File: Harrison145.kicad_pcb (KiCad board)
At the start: 2 copper layers, 85 x 55 mm, 150 parts, among them J1 PITCH ANTENNA, J2 VOLUME ANTENNA, J3 GROUND POINT, J4 LINE OUT, J5 9V IN, Q1 MMBT3906, Q10 SMP5484, Q11 MMBT3906, Q12 MMBT3906, Q13 SMP5484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

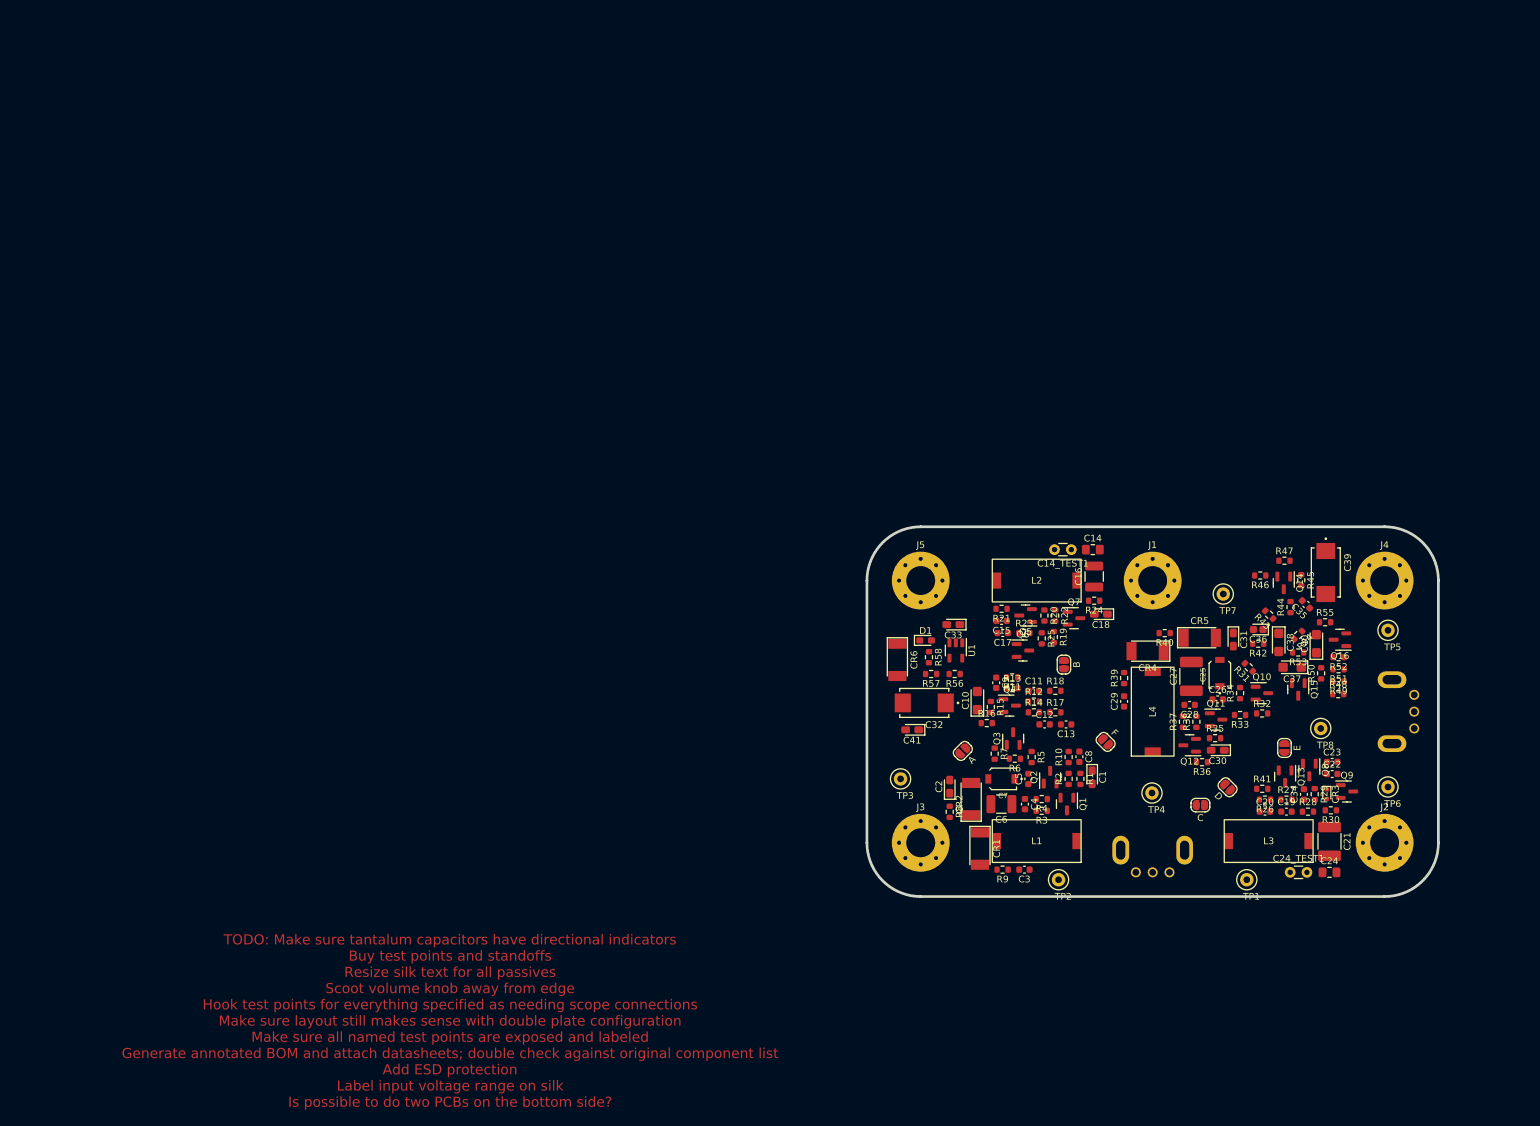
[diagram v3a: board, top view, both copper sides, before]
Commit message: Mostly routed
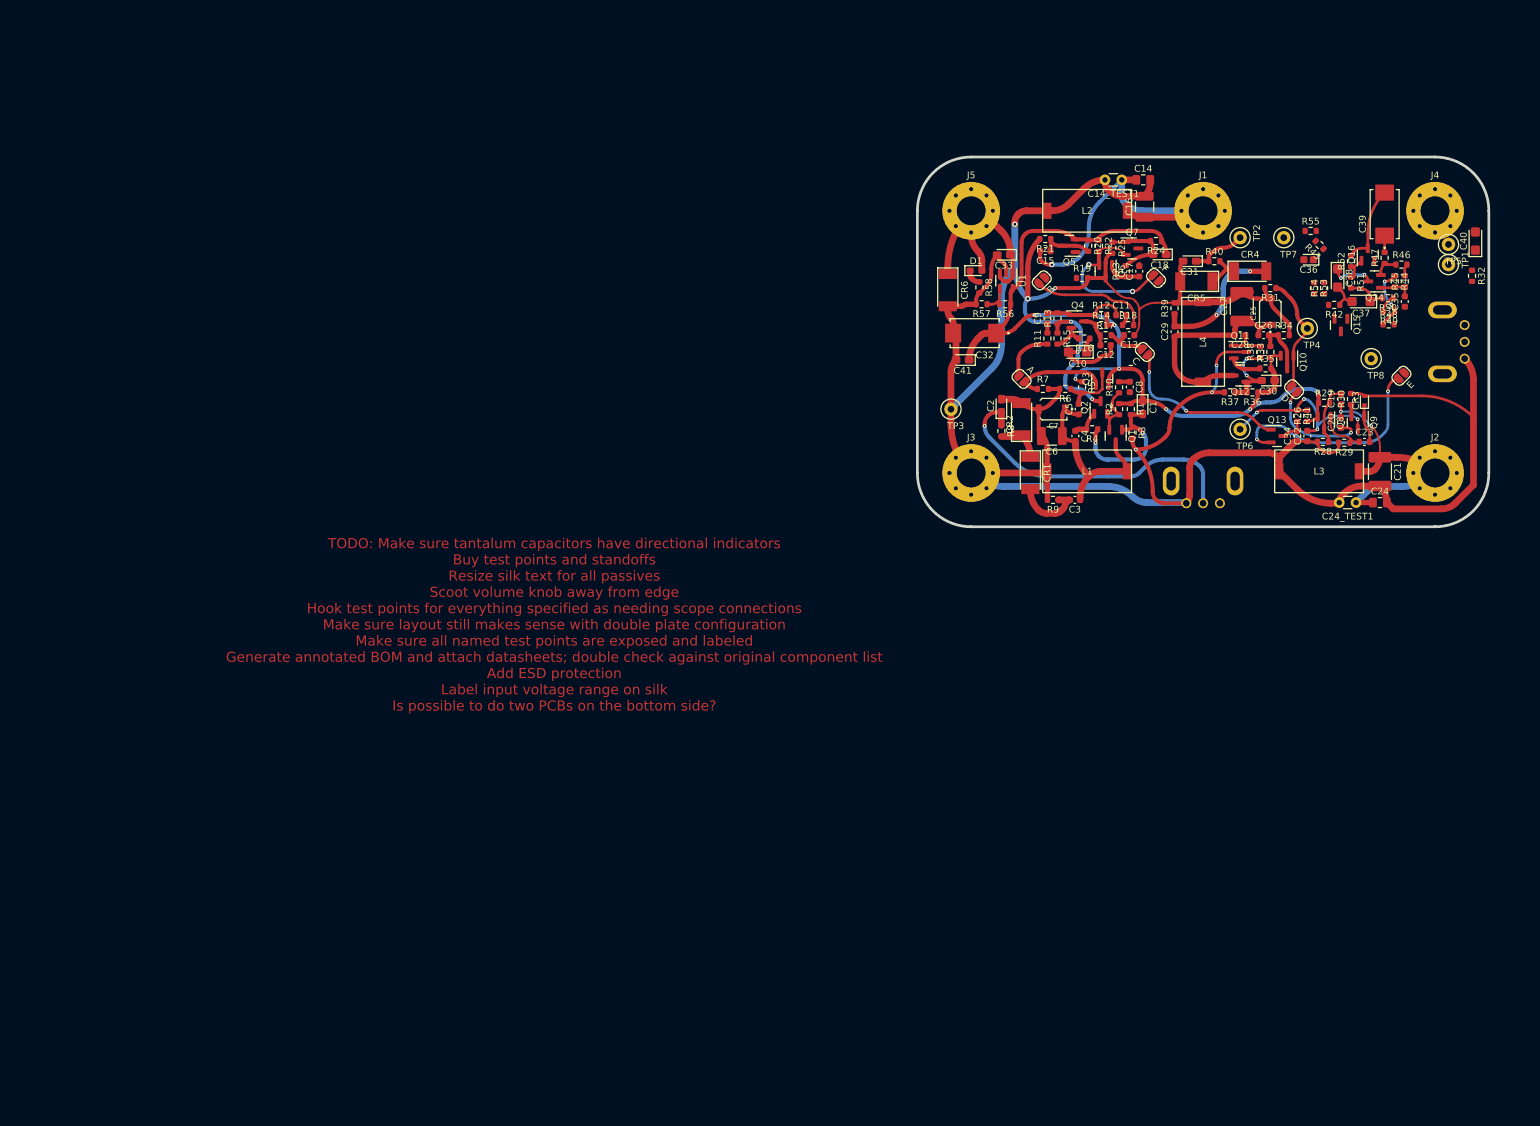
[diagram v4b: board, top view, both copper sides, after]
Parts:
- moved TP2 99.2 mm to (188.5, 64.0), turned to 90 degrees
- moved TP1 96.3 mm to (219.5, 68.0), turned to 90 degrees
- moved RV1 91.5 mm to (221.9, 79.5), turned to -90 degrees
- moved TP4 72.9 mm to (198.5, 77.5)
- moved R32 72.2 mm to (223.0, 69.7), turned to -90 degrees
- moved JP6 69.4 mm to (176.0, 70.0)
- moved JP3 67.9 mm to (174.3, 81.0), turned to -45 degrees
- moved C40 64.4 mm to (223.5, 64.5)
- moved C19 61.9 mm to (203.5, 88.0), turned to 90 degrees
- moved R30 61.2 mm to (205.0, 88.0), turned to 90 degrees
- moved JP4 60.0 mm to (196.5, 86.5)
- moved R27 59.3 mm to (201.0, 88.6)
- moved R25 59.0 mm to (169.5, 65.5)
- moved R16 59.0 mm to (165.3, 79.0), turned to 180 degrees
- moved C20 59.0 mm to (203.5, 91.5), turned to 90 degrees
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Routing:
- net GND: track 0.00 -> 452.2 mm, vias 0 -> 9
- net +7.5V: track 0.00 -> 152.5 mm, vias 0 -> 9
- net Net-(C14-Pad1): track 0.00 -> 54.7 mm, vias 0 -> 1
- net Net-(C2-Pad1): track 0.00 -> 47.6 mm, vias 0 -> 1
- net Net-(C19-Pad1): track 0.00 -> 41.1 mm, vias 0 -> 2
- net +9V: track 0.00 -> 35.7 mm
- net E: track 0.00 -> 32.8 mm, vias 0 -> 2
- net Net-(C25-Pad1): track 0.00 -> 31.8 mm
- net Net-(C3-Pad1): track 0.00 -> 28.7 mm
- net Net-(C22-Pad2): track 0.00 -> 28.5 mm, vias 0 -> 4
- net C: track 0.00 -> 25.3 mm, vias 0 -> 2
- net F: track 0.00 -> 23.0 mm, vias 0 -> 2
- net Net-(C1-Pad2): track 0.00 -> 21.8 mm, vias 0 -> 2
- net Net-(C29-Pad2): track 0.00 -> 20.6 mm, vias 0 -> 2
- net Net-(Q10-Pad1): track 0.00 -> 18.2 mm
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
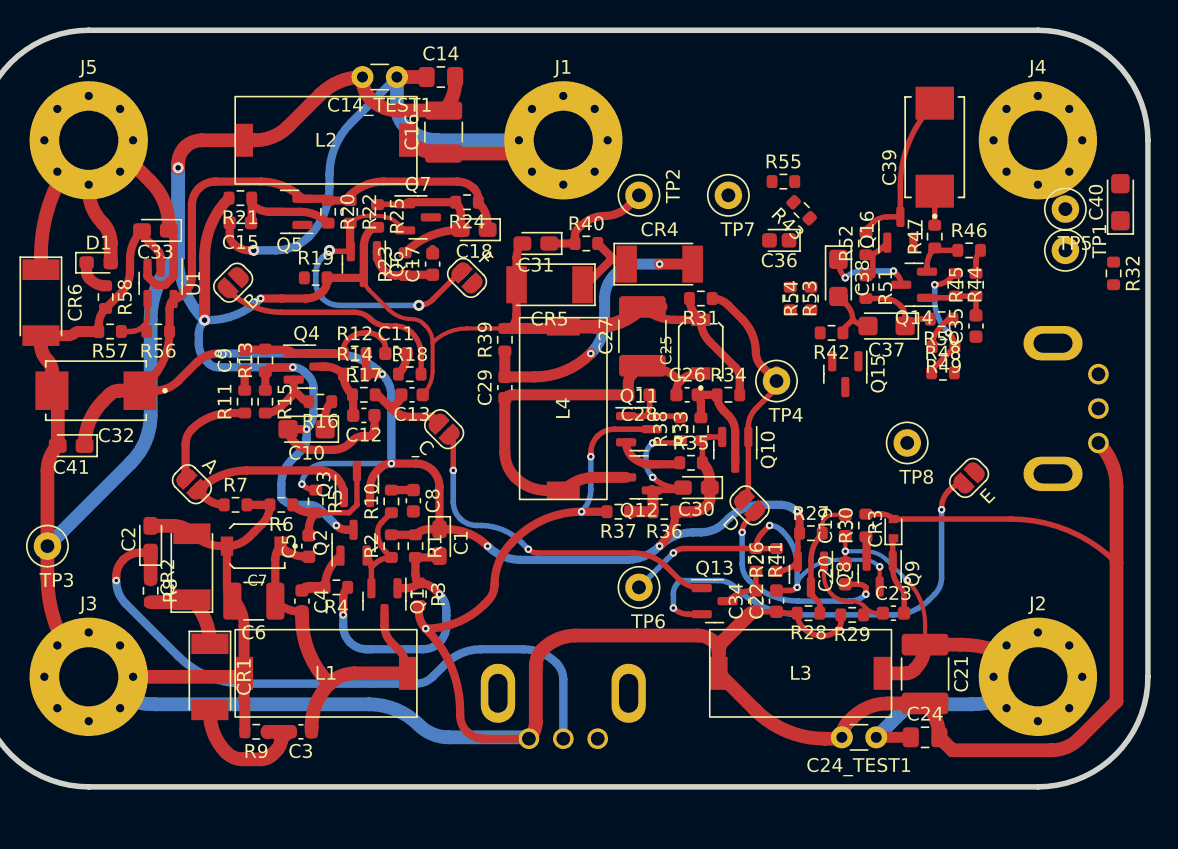
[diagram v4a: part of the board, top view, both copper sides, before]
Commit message: Routing finished, still needs to pass DRC
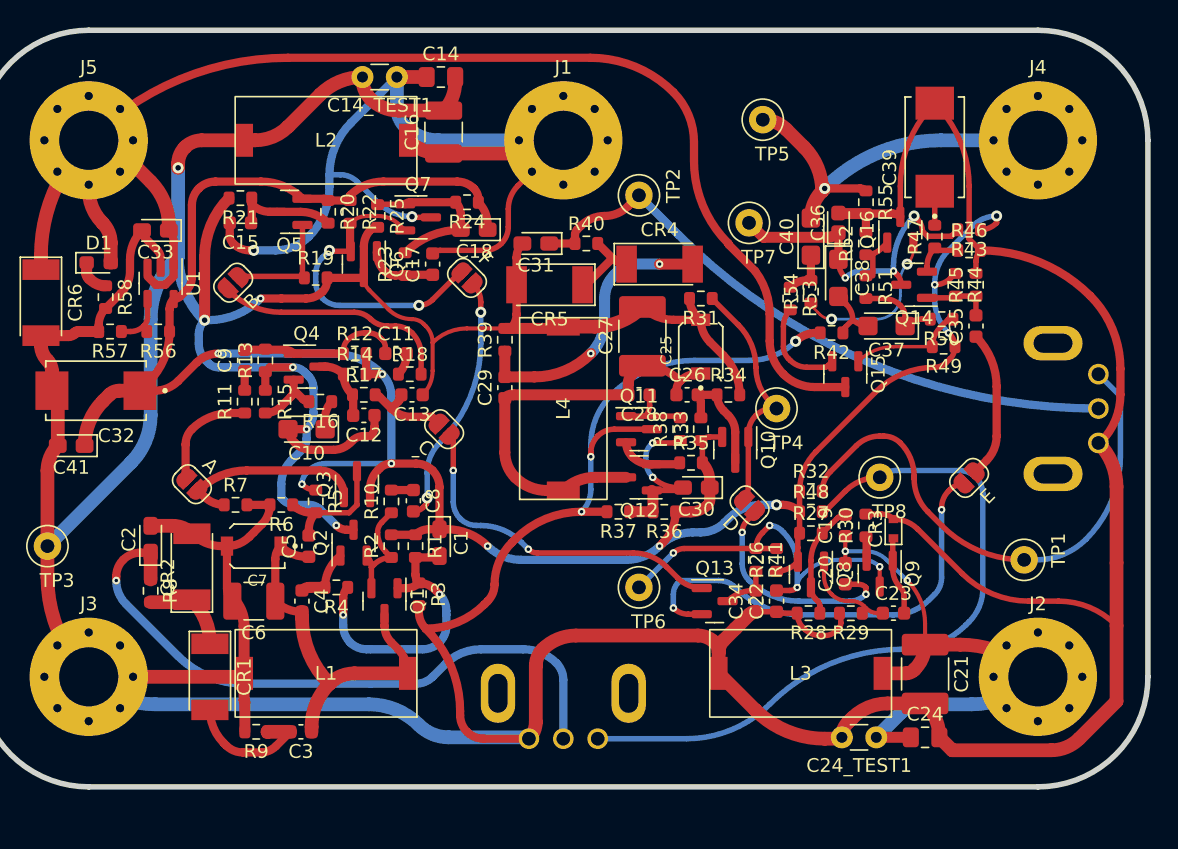
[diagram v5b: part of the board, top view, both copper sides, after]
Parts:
- moved R32 27.1 mm to (201.0, 85.5), turned to 0 degrees
- moved TP5 22.9 mm to (197.5, 58.5)
- moved TP1 22.7 mm to (216.5, 90.5)
- moved C40 22.6 mm to (201.0, 67.0)
- moved R48 13.9 mm to (201.0, 87.0)
- moved R43 12.3 mm to (212.5, 66.5), turned to 180 degrees
- moved R55 6.18 mm to (205.0, 64.5), turned to -90 degrees
- moved C36 4.49 mm to (203.0, 66.0), turned to 90 degrees
- moved TP8 3.20 mm to (206.0, 84.5)
- moved TP7 2.50 mm to (196.5, 66.0)
- moved TP4 2.00 mm to (198.5, 79.5)
- moved R54 0.50 mm to (201.0, 71.0)
- moved R29 0.16 mm to (203.9, 94.4)
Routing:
- net +9V: track 35.7 -> 106.4 mm
- net GND: track 452.2 -> 507.2 mm
- net Net-(R48-Pad2): track 0.00 -> 52.3 mm
- net Net-(R32-Pad2): track 0.00 -> 39.4 mm
- net Net-(C31-Pad1): track 8.22 -> 46.0 mm
- net Net-(C40-Pad2): track 0.00 -> 29.1 mm, vias 0 -> 1
- net +7.5V: track 152.5 -> 176.9 mm, vias 9 -> 10
- net Net-(C14-Pad1): track 54.7 -> 77.2 mm, vias 1 -> 2
- net Net-(C8-Pad2): track 0.00 -> 18.2 mm, vias 0 -> 2
- net Net-(C36-Pad1): track 6.28 -> 23.8 mm, vias 2 -> 3
- net Net-(Q16-Pad2): track 0.00 -> 12.1 mm, vias 0 -> 2
- net Net-(C35-Pad1): track 0.00 -> 10.7 mm
- net B: track 0.00 -> 8.63 mm
- net Net-(Q15-Pad2): track 0.00 -> 7.29 mm
- net Net-(Q15-Pad1): track 2.72 -> 8.36 mm
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
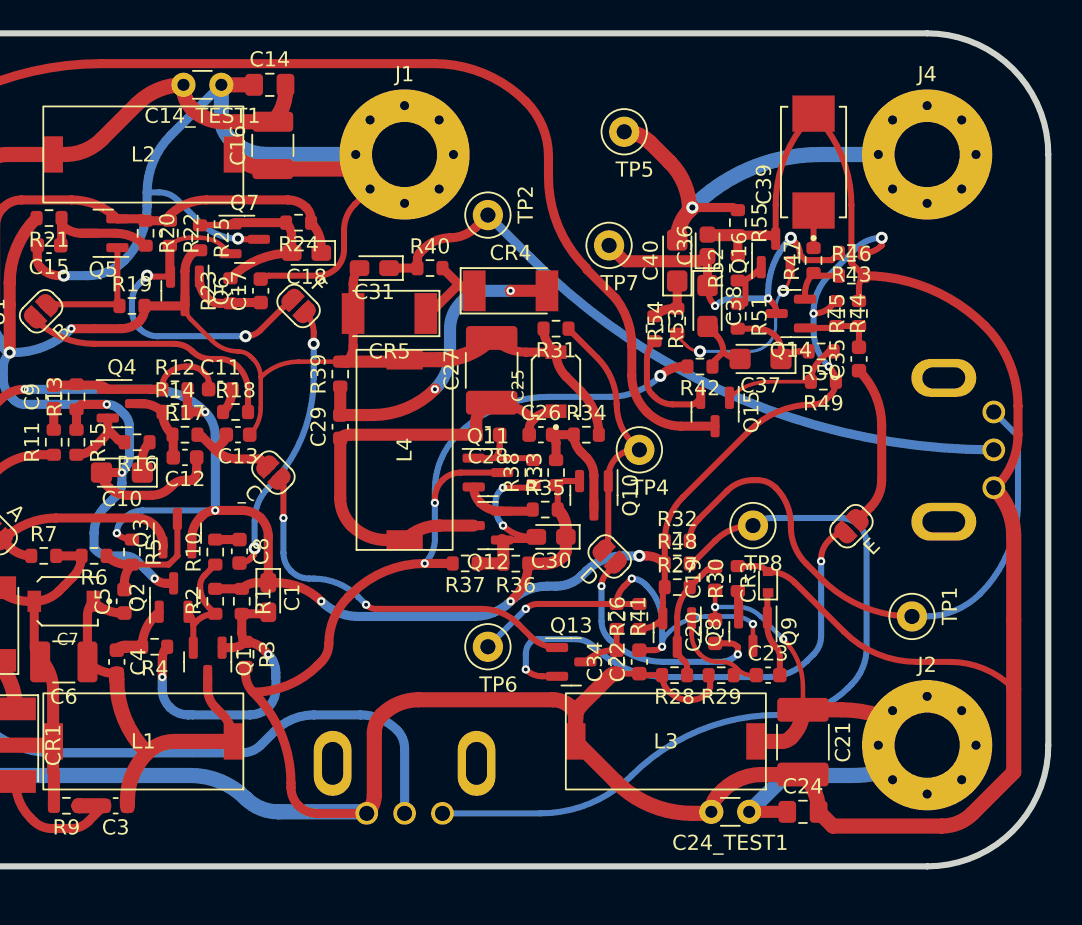
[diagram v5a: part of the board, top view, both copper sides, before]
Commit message: Improved DRC
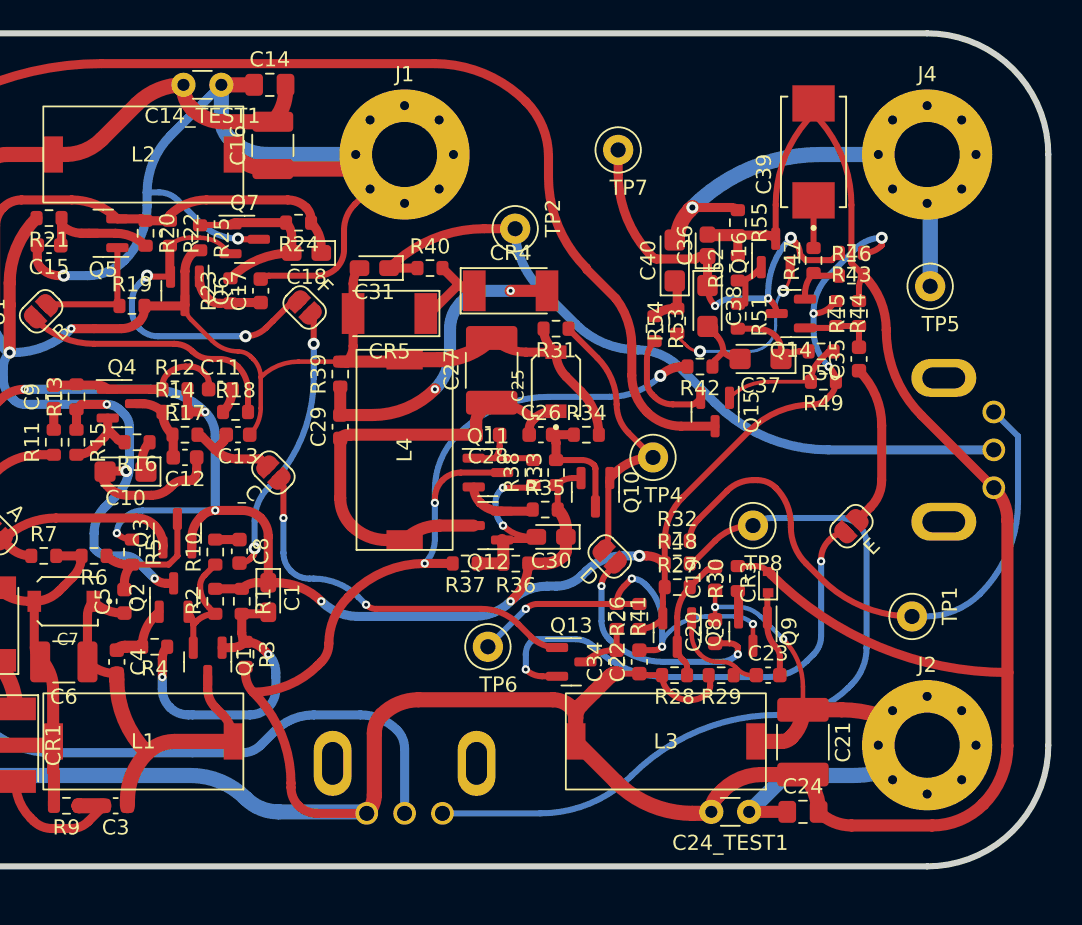
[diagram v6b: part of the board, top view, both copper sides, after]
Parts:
- moved TP5 22.6 mm to (217.7, 68.7)
- moved TP7 6.33 mm to (197.1, 59.7)
- moved TP2 2.01 mm to (190.3, 64.9)
- moved TP4 1.03 mm to (199.4, 80.0)
- moved C39 0.67 mm to (210.0, 59.8)
- moved JP6 0.41 mm to (176.4, 70.1)
- moved C10 0.25 mm to (164.6, 80.9)
- moved Q10 0.22 mm to (195.6, 82.3)
- moved C40 0.16 mm to (200.8, 67.0)
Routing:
- net GND: track 507.2 -> 502.2 mm
- net Net-(C36-Pad1): track 23.8 -> 28.2 mm
- net Net-(C31-Pad1): track 46.0 -> 48.6 mm
- net Net-(C40-Pad2): track 29.1 -> 30.6 mm
- net Net-(Q10-Pad1): track 17.5 -> 18.5 mm
